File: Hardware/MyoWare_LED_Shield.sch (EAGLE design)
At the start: 16 parts, among them IC1 LM3914V

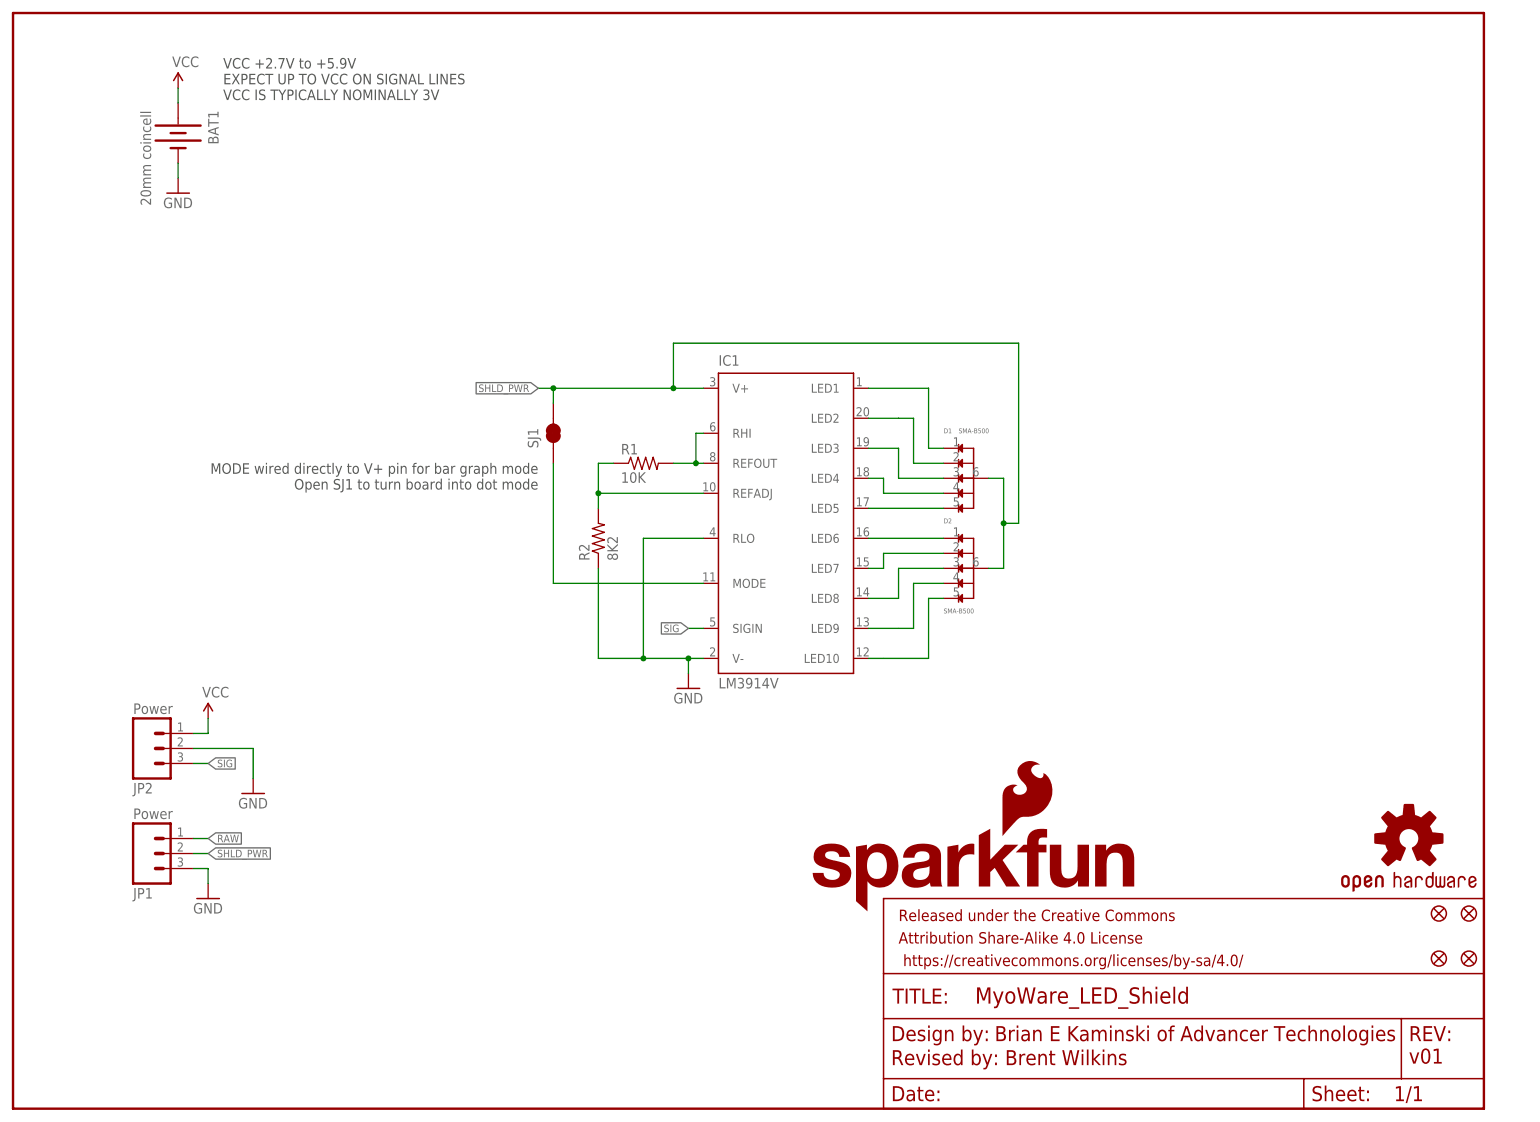
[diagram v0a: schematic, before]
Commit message: Started move to LiPo based design
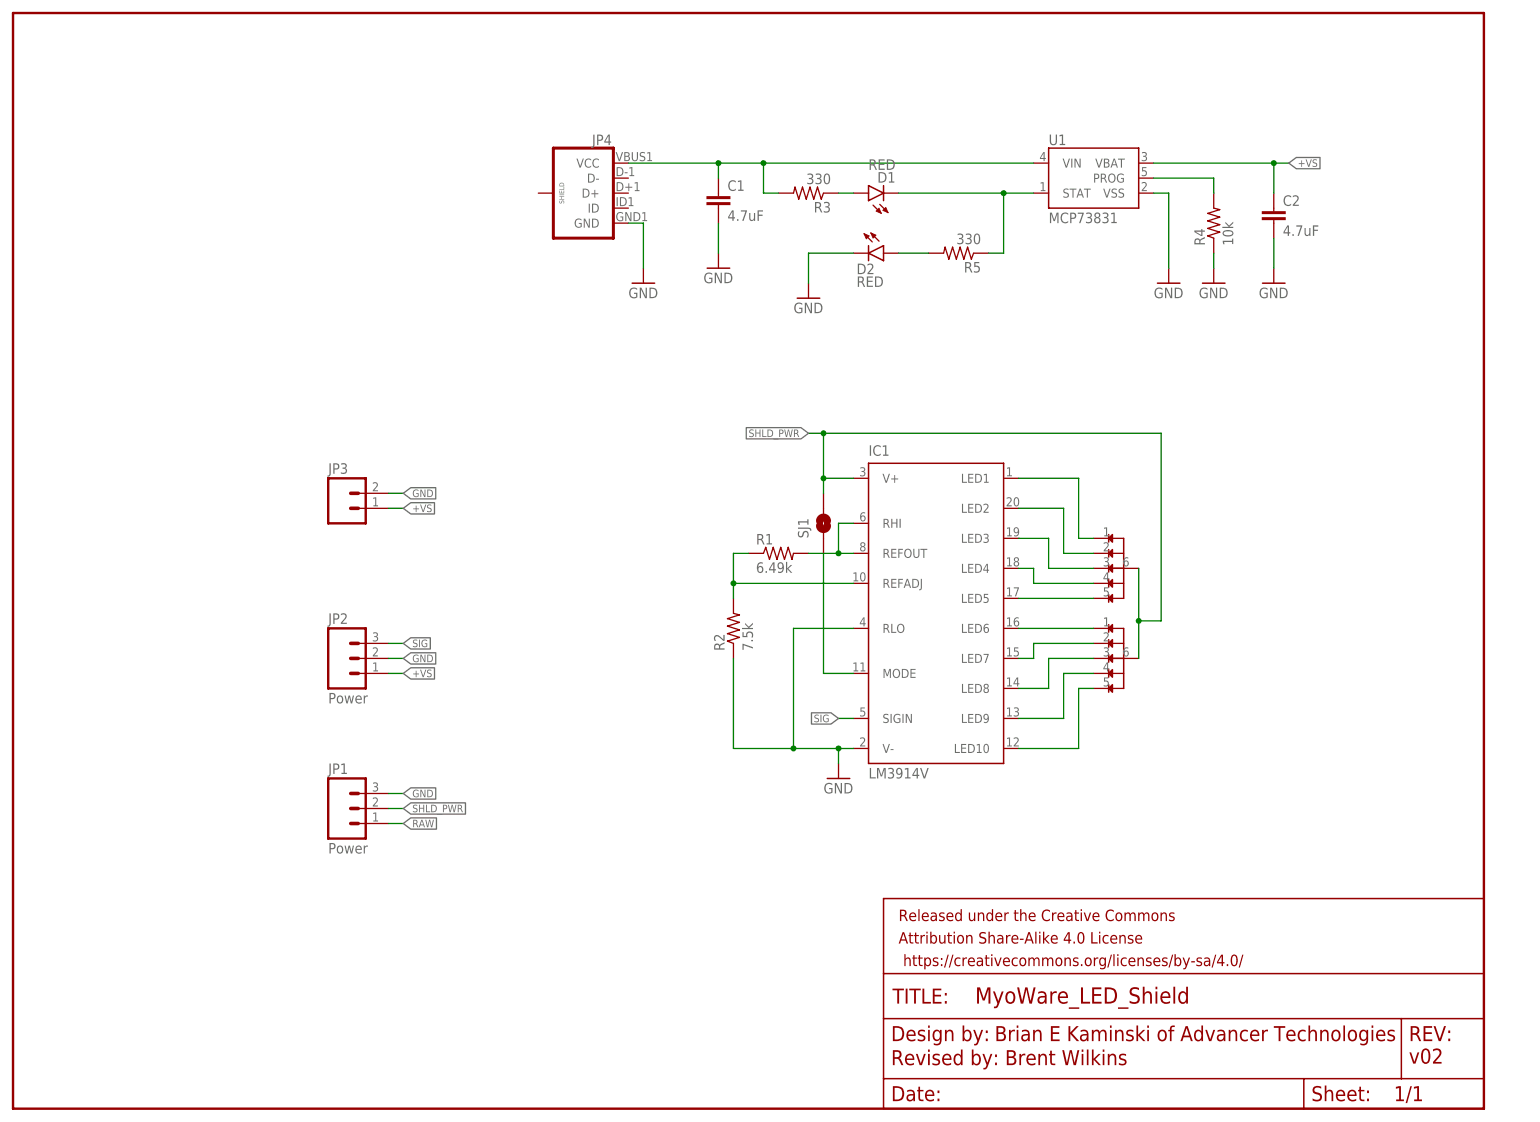
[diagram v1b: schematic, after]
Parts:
- removed BAT1: 20mm coincell, SparkFun-Electromechanical:BATTERY20MM_4LEGS
- removed FID1, FID2, FID3, FID4: FIDUCIAL1X2, SparkFun-Aesthetics:FIDUCIAL1X2
- removed LOGO1: SFE_LOGO_NAME_FLAME.1_INCH, SparkFun-Aesthetics:SFE_LOGO_NAME_FLAME.1_INCH
- removed LOGO2: OSHW-LOGOS, SparkFun-Aesthetics:OSHW-LOGOS
- added C1, C2: 4.7uF, SparkFun-Capacitors:4.7UF-6.3V-10%(0603)0603
- added JP3: (no value), SparkFun-Connectors:M021X02_NO_SILK
- added JP4: (no value), SparkFun-Connectors:USB_MICROB_PLUGCONN-11752
- added R3, R5: 330, resistor:R-US_R0603
- added R4: 10k, resistor:R-US_R0603
- added U$1, U$2: SMA-B500, advancer-technologies:SMA-B500
- added U1: MCP73831, SparkFun-PowerIC:MCP73831
- D1, D2: value SMA-B500 -> RED; device Testing:SMA-B500 -> SparkFun-LED:LED-RED0603; PROD_ID DIO-13127 -> (none)
- IC1: device Testing:LM3914V -> national-semiconductor:LM3914V; PROD_ID IC-13110 -> (none)
- R1: value 10K -> 6.49k; device SparkFun-Resistors:10KOHM-1/10W-1%(0603)0603 -> resistor:R-US_R0603
- R2: value 8K2 -> 7.5k; device SparkFun-Resistors:8.2KOHM-1/10W-5%(0603) -> resistor:R-US_R0603
- SJ1: value JUMPER-PAD-2-NC_BY_TRACE -> SOLDERJUMPERTRACE; device SparkFun-Passives:JUMPER-PAD-2-NC_BY_TRACE -> SparkFun:SOLDERJUMPERTRACE
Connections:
- removed net VCC: BAT1.+, JP2.1
- new net +VS: C2.1, JP2.1, JP3.1, U1.VBAT
- new net N$10: D1.A, R3.1
- new net N$15: D1.C, R5.1, U1.STAT
- new net N$17: R4.2, U1.PROG
- new net N$7: C1.1, JP4.VCC, R3.2, U1.VIN
- new net N$9: D2.A, R5.2
- net GND: now also C1.2, C2.2, D2.C, JP3.2, JP4.GND, R4.1, U1.VSS; no longer BAT1.-
- net N$1: now also U$1.1; no longer D1.1
- net N$11: now also U$2.2; no longer D2.2
- net N$12: now also U$2.3; no longer D2.3
- net N$13: now also U$2.4; no longer D2.4
- net N$14: now also U$2.5; no longer D2.5
- net N$2: now also U$1.2; no longer D1.2
- net N$3: now also U$1.5; no longer D1.5
- net N$4: now also U$1.3; no longer D1.3
- net N$5: now also U$2.1; no longer D2.1
- net N$8: now also U$1.4; no longer D1.4
- net SHLD_PWR: now also U$1.6, U$2.6; no longer D1.6, D2.6
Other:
- note added: "v02"
- note removed: "MODE wired directly to V+ pin for bar graph mode Open SJ1 to turn board into dot mode"
- note removed: "VCC +2.7V to +5.9V EXPECT UP TO VCC ON SIGNAL LINES VCC IS TYPICALLY NOMINALLY 3V"
- note removed: "v01"
- moved on the sheet: IC1, JP1, JP2, R1, R2

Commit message: Design rules checked
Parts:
- removed IC1: LM3914V, national-semiconductor:LM3914V
- removed SJ1: SOLDERJUMPERTRACE, SparkFun:SOLDERJUMPERTRACE
- removed U$1, U$2: SMA-B500, advancer-technologies:SMA-B500
- added D3, D4: SMA-B500, Testing:SMA-B500
- added FID1, FID2, FID3, FID4: FIDUCIAL1X2, SparkFun-Aesthetics:FIDUCIAL1X2
- added LOGO1: SFE_LOGO_FLAME.1_INCH, SparkFun-Aesthetics:SFE_LOGO_FLAME.1_INCH
- added LOGO2: OSHW-LOGOS, SparkFun-Aesthetics:OSHW-LOGOS
- added MODE: JUMPER-PAD-2-NC_BY_TRACE, SparkFun-Passives:JUMPER-PAD-2-NC_BY_TRACE
- added U2: LM3914V, Testing:LM3914V
- JP2: value Power -> Signal
- JP3: value (none) -> LiPo
- R1: PROD_ID (none) -> RES-13202
- R2: PROD_ID (none) -> RES-13203
- R3, R5: device resistor:R-US_R0603 -> SparkFun-Resistors:330OHM1/10W1%(0603)
- R4: value 10k -> 10K; device resistor:R-US_R0603 -> SparkFun-Resistors:10KOHM-1/10W-1%(0603)0603
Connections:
- net N$7 renamed VBUS
- net GND: now also U2.RLO, U2.V-; no longer IC1.RLO, IC1.V-
- net N$1: now also D3.1, U2.LED1; no longer IC1.LED1, U$1.1
- net N$11: now also D4.2, U2.LED7; no longer IC1.LED7, U$2.2
- net N$12: now also D4.3, U2.LED8; no longer IC1.LED8, U$2.3
- net N$13: now also D4.4, U2.LED9; no longer IC1.LED9, U$2.4
- net N$14: now also D4.5, U2.LED10; no longer IC1.LED10, U$2.5
- net N$19: now also U2.REFADJ; no longer IC1.REFADJ
- net N$2: now also D3.2, U2.LED2; no longer IC1.LED2, U$1.2
- net N$20: now also U2.REFOUT, U2.RHI; no longer IC1.REFOUT, IC1.RHI
- net N$3: now also D3.5, U2.LED5; no longer IC1.LED5, U$1.5
- net N$4: now also D3.3, U2.LED3; no longer IC1.LED3, U$1.3
- net N$5: now also D4.1, U2.LED6; no longer IC1.LED6, U$2.1
- net N$6: now also MODE.1, U2.MODE; no longer IC1.MODE, SJ1.1
- net N$8: now also D3.4, U2.LED4; no longer IC1.LED4, U$1.4
- net SHLD_PWR: now also D3.6, D4.6, MODE.2, U2.V+; no longer IC1.V+, SJ1.2, U$1.6, U$2.6
- net SIG: now also U2.SIGIN; no longer IC1.SIGIN
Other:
- note added: "+VS +2.7V to +5.9V EXPECT UP TO VCC ON SIGNAL LINES +VS IS TYPICALLY NOMINALLY 3.7V"
- note added: "BATTERY CHARGER"
- note added: "LED CONTROL"
- note added: "MODE wired directly to V+ pin for bar graph mode Open SJ1 to turn board into dot mode"
- note added: "PTH CONNECTIONS"
- moved on the sheet: C1, JP1, JP2, JP3, R1, R2

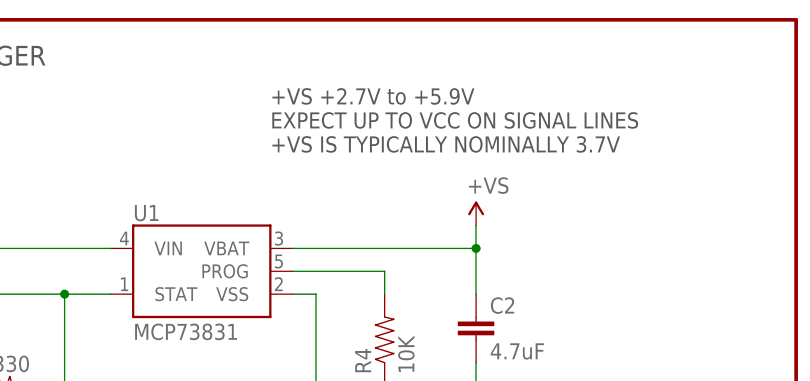
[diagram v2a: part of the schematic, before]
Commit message: Adjusted max +VS
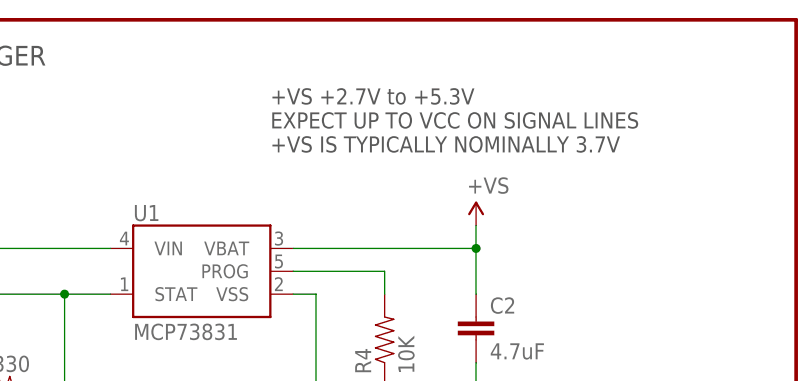
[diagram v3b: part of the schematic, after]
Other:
- note added: "+VS +2.7V to +5.3V EXPECT UP TO VCC ON SIGNAL LINES +VS IS TYPICALLY NOMINALLY 3.7V"
- note removed: "+VS +2.7V to +5.9V EXPECT UP TO VCC ON SIGNAL LINES +VS IS TYPICALLY NOMINALLY 3.7V"
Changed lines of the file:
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@@
 <text x="148.59" y="7.366" size="2.54" layer="94" ratio="10">Revised by: Brent Wilkins</text>
 <text x="236.22" y="7.62" size="2.54" layer="94" font="vector">v02</text>
-<text x="190.5" y="177.8" size="1.778" layer="97" font="vector" ratio="15" align="top-left">+VS +2.7V to +5.9V
+<text x="190.5" y="177.8" size="1.778" layer="97" font="vector" ratio="15" align="top-left">+VS +2.7V to +5.3V
 EXPECT UP TO VCC ON SIGNAL LINES
 +VS IS TYPICALLY NOMINALLY 3.7V</text>

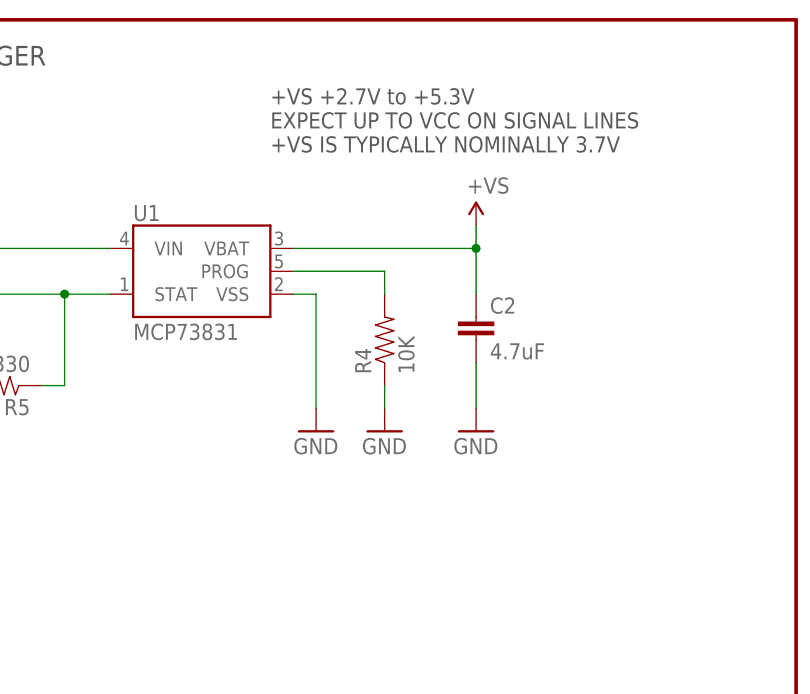
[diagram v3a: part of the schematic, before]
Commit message: Tweaks (mostly silk and info)
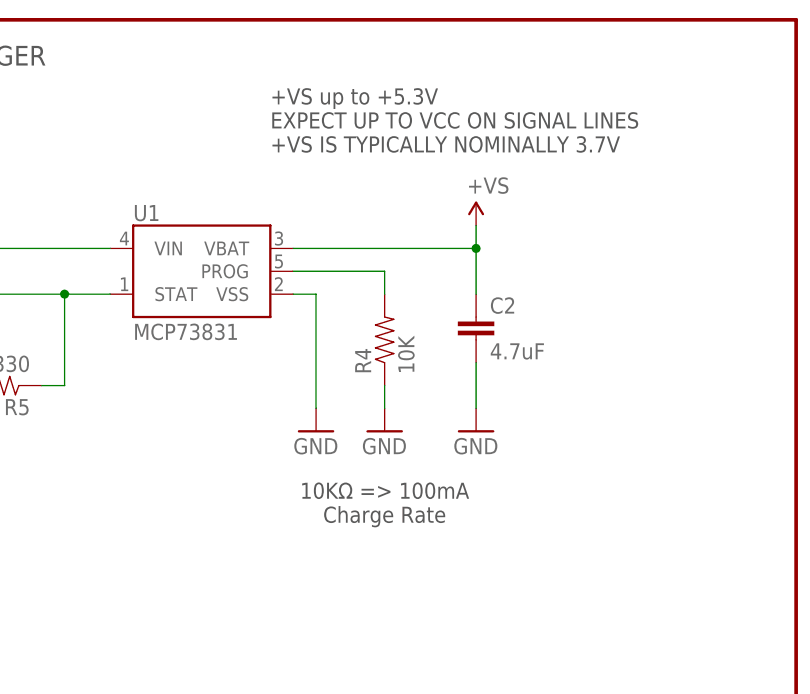
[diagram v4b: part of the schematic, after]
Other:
- note added: "+VS up to +5.3V EXPECT UP TO VCC ON SIGNAL LINES +VS IS TYPICALLY NOMINALLY 3.7V"
- note added: "10KΩ => 100mA Charge Rate"
- note removed: "+VS +2.7V to +5.3V EXPECT UP TO VCC ON SIGNAL LINES +VS IS TYPICALLY NOMINALLY 3.7V"
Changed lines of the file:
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@@
 <text x="148.59" y="7.366" size="2.54" layer="94" ratio="10">Revised by: Brent Wilkins</text>
 <text x="236.22" y="7.62" size="2.54" layer="94" font="vector">v02</text>
-<text x="190.5" y="177.8" size="1.778" layer="97" font="vector" ratio="15" align="top-left">+VS +2.7V to +5.3V
+<text x="190.5" y="177.8" size="1.778" layer="97" font="vector" ratio="15" align="top-left">+VS up to +5.3V
 EXPECT UP TO VCC ON SIGNAL LINES
 +VS IS TYPICALLY NOMINALLY 3.7V</text>
@@
 <text x="152.4" y="180.34" size="2.1844" layer="97" font="vector" ratio="15" align="bottom-center">BATTERY CHARGER</text>
 <text x="127" y="101.6" size="2.1844" layer="97" font="vector" ratio="15" align="bottom-center">LED CONTROL</text>
+<text x="203.2" y="129.54" size="1.778" layer="97" font="vector" ratio="15" align="bottom-center">10KΩ =&gt; 100mA
+Charge Rate</text>
 </plain>
 <instances>

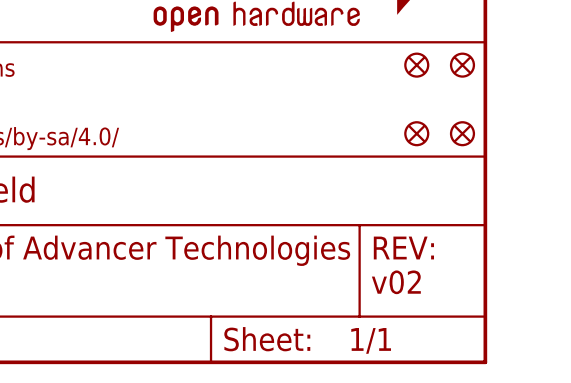
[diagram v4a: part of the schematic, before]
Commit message: Moved charge LEDs to back of board from easier manufacturing
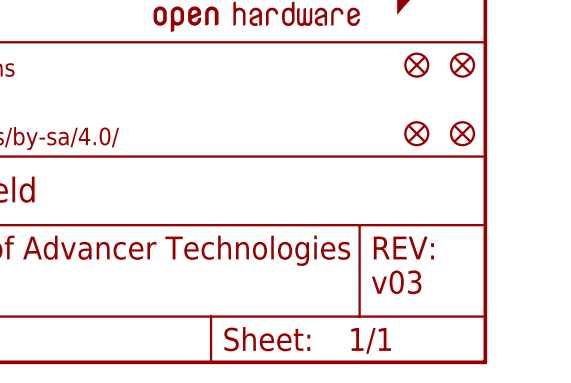
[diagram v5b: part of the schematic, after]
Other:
- note added: "v03"
- note removed: "v02"
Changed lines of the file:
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@@
 <?xml version="1.0" encoding="utf-8"?>
 <!DOCTYPE eagle SYSTEM "eagle.dtd">
-<eagle version="7.4.0">
+<eagle version="7.5.0">
 <drawing>
 <settings>
@@
 <text x="166.116" y="11.43" size="2.54" layer="94">Brian E Kaminski of Advancer Technologies</text>
 <text x="148.59" y="7.366" size="2.54" layer="94" ratio="10">Revised by: Brent Wilkins</text>
-<text x="236.22" y="7.62" size="2.54" layer="94" font="vector">v02</text>
+<text x="236.22" y="7.62" size="2.54" layer="94" font="vector">v03</text>
 <text x="190.5" y="177.8" size="1.778" layer="97" font="vector" ratio="15" align="top-left">+VS up to +5.3V
 EXPECT UP TO VCC ON SIGNAL LINES

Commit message: Added cable header alignment in silk & minor weaks.
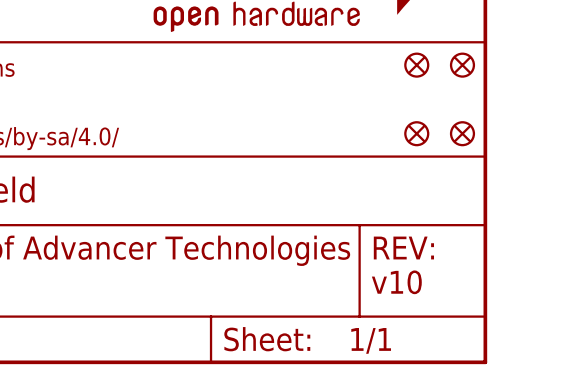
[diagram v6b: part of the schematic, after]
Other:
- note added: "v10"
- note removed: "v03"
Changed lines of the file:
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@@
 <text x="166.116" y="11.43" size="2.54" layer="94">Brian E Kaminski of Advancer Technologies</text>
 <text x="148.59" y="7.366" size="2.54" layer="94" ratio="10">Revised by: Brent Wilkins</text>
-<text x="236.22" y="7.62" size="2.54" layer="94" font="vector">v03</text>
+<text x="236.22" y="7.62" size="2.54" layer="94" font="vector">v10</text>
 <text x="190.5" y="177.8" size="1.778" layer="97" font="vector" ratio="15" align="top-left">+VS up to +5.3V
 EXPECT UP TO VCC ON SIGNAL LINES
